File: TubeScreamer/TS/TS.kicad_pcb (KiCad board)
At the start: 2 copper layers, 80 parts, among them J1 DC 9V, J2 BAT, J3 IN, J4 OUT, Q1 2SC1815, Q2 2SK44SP, Q3 2SC1815, Q4 2SC1815, Q5 2SC1815, Q6 2SC1815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

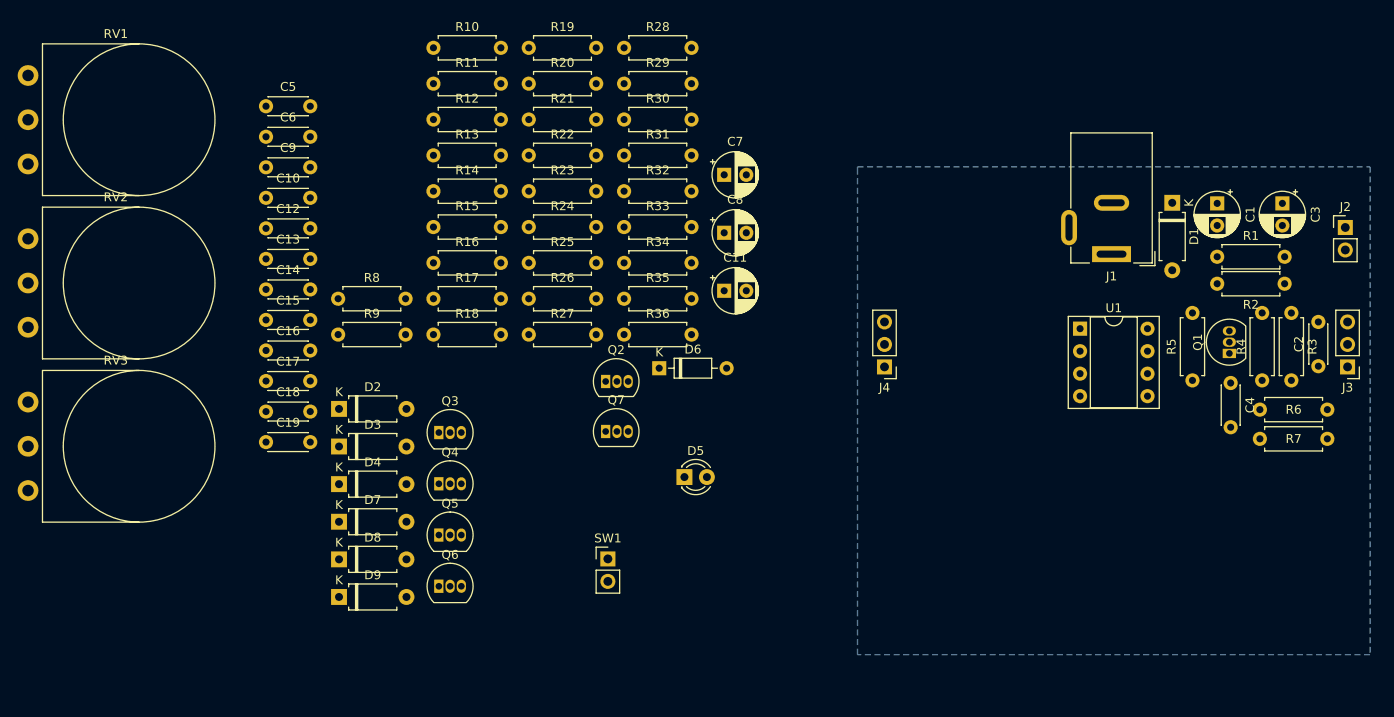
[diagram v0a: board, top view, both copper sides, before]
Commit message: Update 27_03_15
sch TS fix
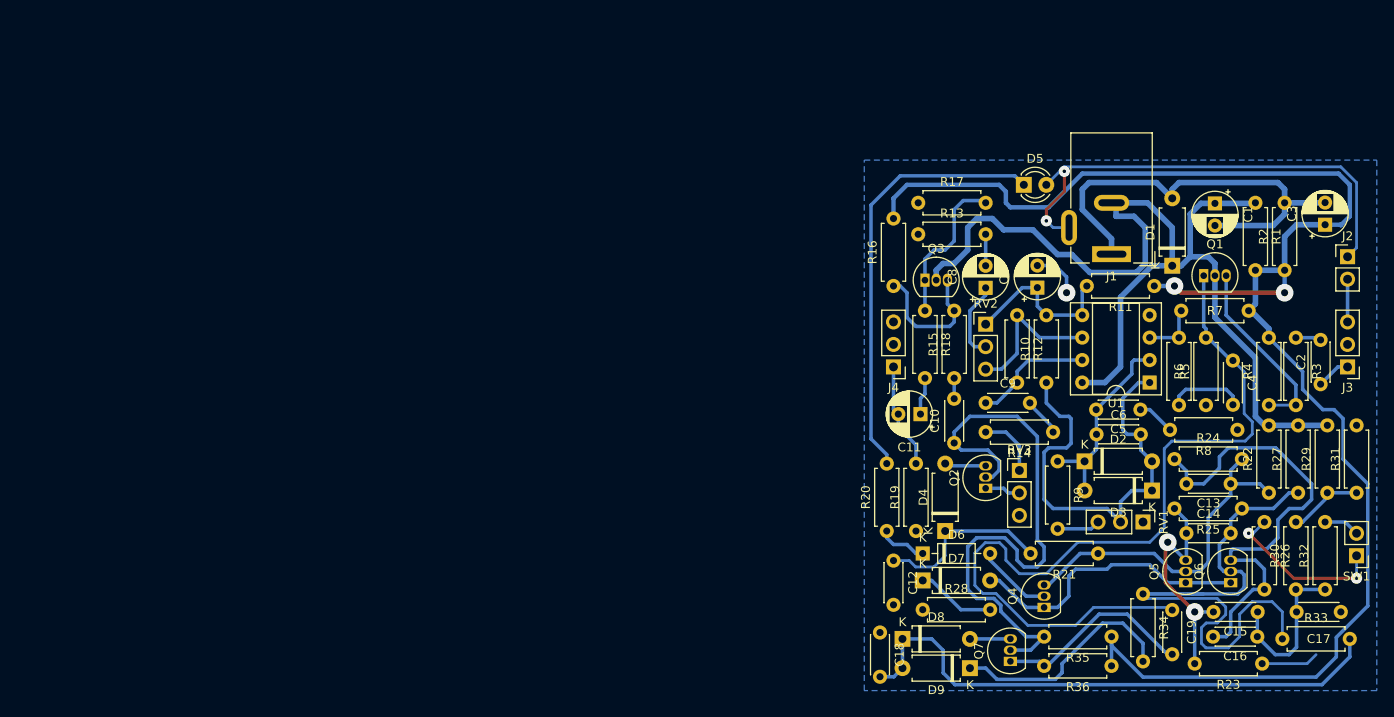
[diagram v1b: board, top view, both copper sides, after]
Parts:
- RV1, RV2, RV3: footprint Potentiometer_THT:Potentiometer_Omeg_PC16BU_Vertical -> Connector_PinHeader_2.54mm:PinHeader_1x03_P2.54mm_Vertical
- moved RV1 132.3 mm to (173.0, 77.5), turned to -90 degrees
- moved C17 124.2 mm to (195.3, 87.6), turned to 180 degrees
- moved C15 116.8 mm to (185.9, 87.6), turned to 180 degrees
- moved C16 116.6 mm to (185.9, 90.4), turned to 180 degrees
- moved RV3 112.0 mm to (159.0, 71.6)
- moved C13 111.9 mm to (182.9, 73.2), turned to 180 degrees
- moved RV2 108.2 mm to (155.2, 55.1)
- moved C14 107.6 mm to (177.9, 78.7)
- moved C5 104.6 mm to (172.7, 64.8), turned to 180 degrees
- moved C19 104.1 mm to (176.3, 87.4), turned to -90 degrees
- moved R8 102.7 mm to (183.6, 67.1), turned to 180 degrees
- moved C6 99.7 mm to (167.7, 67.6)
- moved R23 98.6 mm to (186.4, 93.5), turned to 180 degrees
- moved R30 92.6 mm to (190.2, 85.1), turned to 90 degrees
- moved D3 92.0 mm to (174.0, 73.9), turned to 180 degrees
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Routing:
- net 4V5: track 0.00 -> 179.3 mm, vias 0 -> 2
- net 9V: track 0.00 -> 119.9 mm
- net Net-(Q1-E): track 0.00 -> 95.0 mm
- net Net-(Q6-C): track 0.00 -> 71.7 mm
- net Net-(Q2-S): track 0.00 -> 67.3 mm
- net Net-(D8-K): track 0.00 -> 63.2 mm
- net Net-(D5-A): track 0.00 -> 54.7 mm, vias 0 -> 2
- net Net-(Q6-B): track 0.00 -> 53.0 mm
- net Net-(D1-A): track 0.00 -> 50.0 mm
- net Net-(D2-A): track 0.00 -> 49.9 mm
- net Net-(D5-K): track 0.00 -> 49.0 mm
- net Net-(Q4-B): track 0.00 -> 39.3 mm
- net Net-(D7-A): track 0.00 -> 32.6 mm
- net GND: track 0.00 -> 31.3 mm, vias 0 -> 3
- net Net-(Q5-B): track 0.00 -> 26.9 mm, vias 0 -> 2
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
